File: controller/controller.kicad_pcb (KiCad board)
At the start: 4 copper layers, 42.8 x 35.9 mm, 29 parts, among them J1 CONN_04SCREW, U1 10118194-MICRO-USB, U2 LM3671MF-3.3/NOPBMF05A-M, U3 SN74LVC1T45DBVRDBV6-M, U4 SN74LVC1T45DBVRDBV6-M

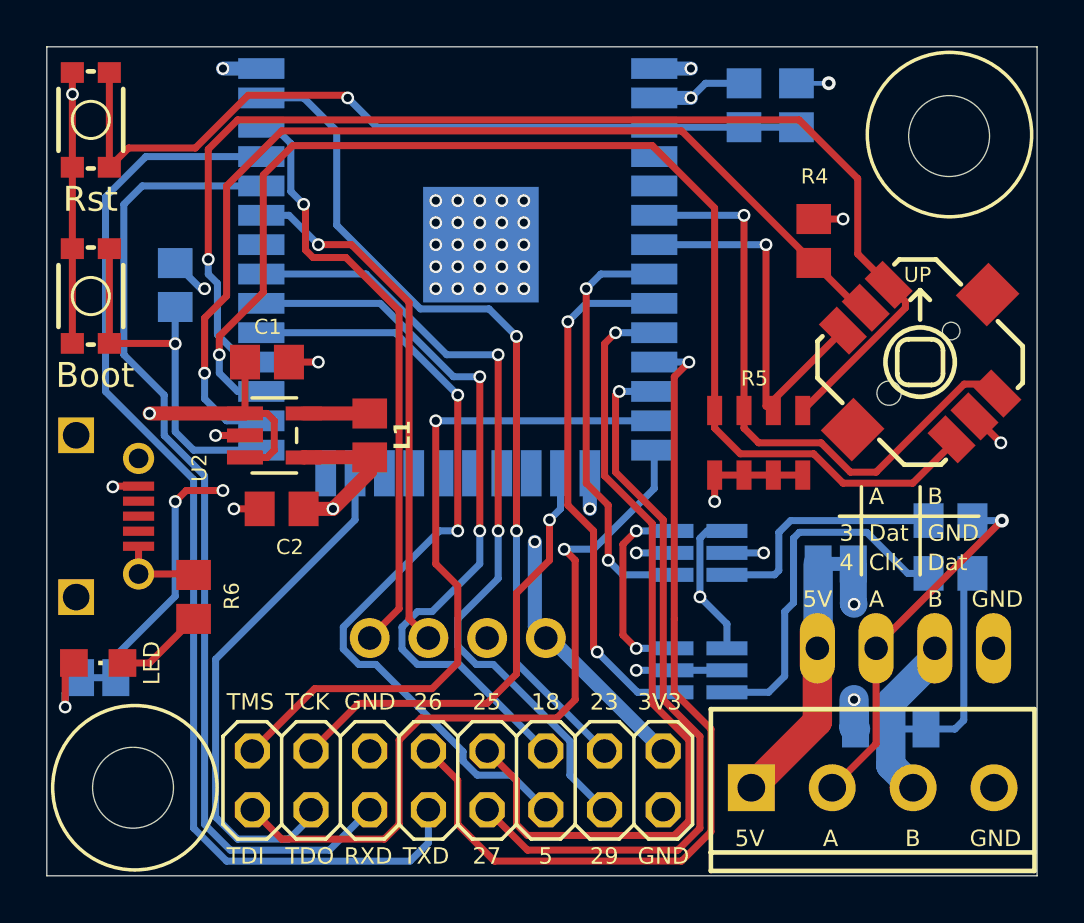
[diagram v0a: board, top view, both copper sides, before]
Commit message: Cleaned up controller
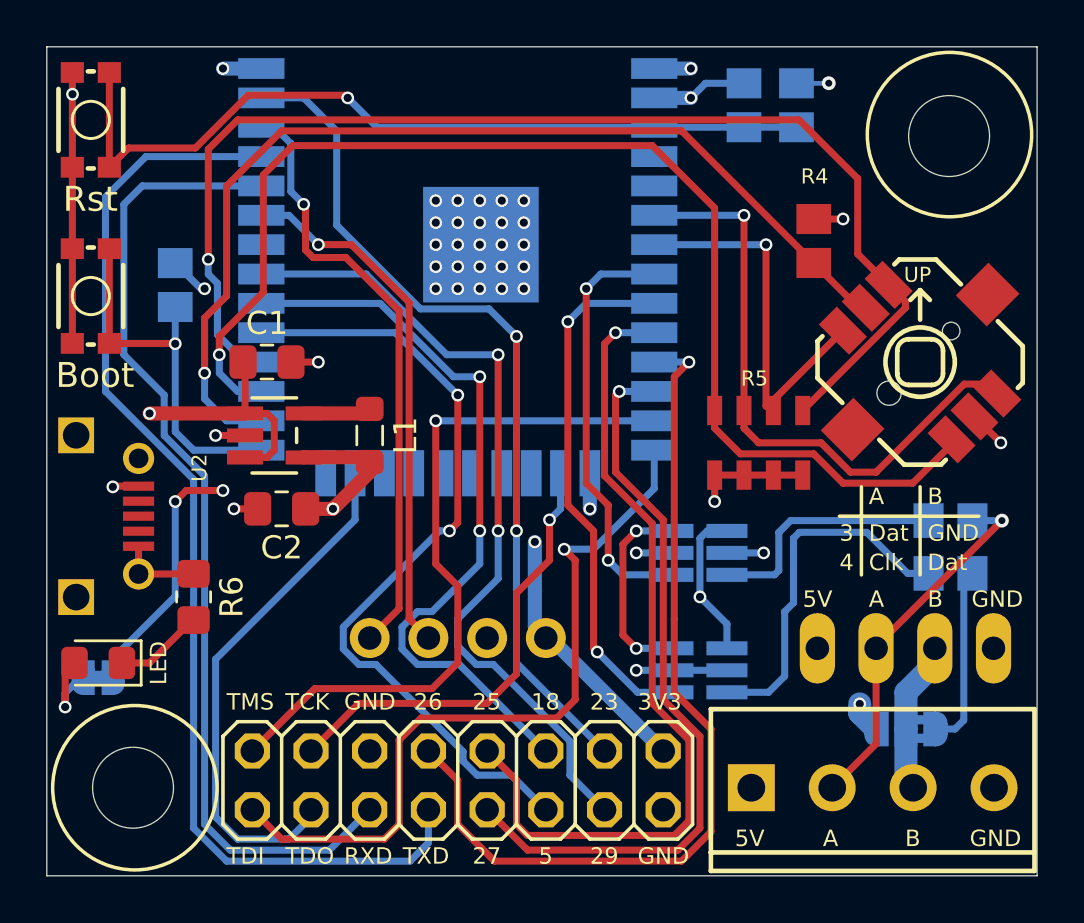
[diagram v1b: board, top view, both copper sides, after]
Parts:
- removed SJ3: SJ, controller:SJ
- C1, C2: footprint controller:C0805 -> Capacitor_SMD:C_0805_2012Metric_Pad1.18x1.45mm_HandSolder
- L1: footprint controller:C0805 -> Inductor_SMD:L_0805_2012Metric_Pad1.05x1.20mm_HandSolder
- LED1: footprint controller:CHIPLED_0805 -> LED_SMD:LED_0805_2012Metric_Pad1.15x1.40mm_HandSolder
- R1, R2: value 220 -> 68
- R6: footprint controller:R0805 -> Resistor_SMD:R_0805_2012Metric_Pad1.20x1.40mm_HandSolder
- SJ1: footprint controller:SJ_2 -> Jumper:SolderJumper-3_P1.3mm_Bridged2Bar12_RoundedPad1.0x1.5mm_NumberLabels
- SJ2: footprint controller:SJ -> Jumper:SolderJumper-2_P1.3mm_Bridged_RoundedPad1.0x1.5mm
- moved SJ1 0.66 mm to (164.2, 116.6)
- turned LED1 to 180 degrees
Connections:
- J1 pad 3: Net-(J1-Pad3) -> Net-(SJ1-C)
- JP1 pad 3: Net-(J1-Pad3) -> Net-(SJ1-C)
- R1 pad 2: Net-(J1-Pad3) -> Net-(SJ1-A)
- R6 pad 2: Net-(LED1-PadC) -> Net-(LED1-K)
- SJ1 pad 1: Net-(J1-Pad3) -> Net-(SJ1-A)
- SJ1 pad 2: Net-(J1-Pad3) -> Net-(SJ1-C)
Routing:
- net Net-(J1-Pad3): track 17.0 -> 0.00 mm
- net +5V: track 32.3 -> 18.1 mm, vias 4 -> 3
- net Net-(SJ1-C): track 0.00 -> 8.01 mm
- net Net-(SJ1-A): track 0.00 -> 7.86 mm
- net Net-(LED1-PadC): track 3.87 -> 0.00 mm
- net Net-(LED1-K): track 0.00 -> 3.87 mm
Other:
- board text added: "RVL Controller v1.8 Copyright Bryan Hughes January 2025"
- board text removed: "RVL Controller v1.7 Copyright Bryan Hughes June 2024"
